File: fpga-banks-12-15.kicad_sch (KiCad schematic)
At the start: 1 part, among them U1 XC7K410T-2FFG900I

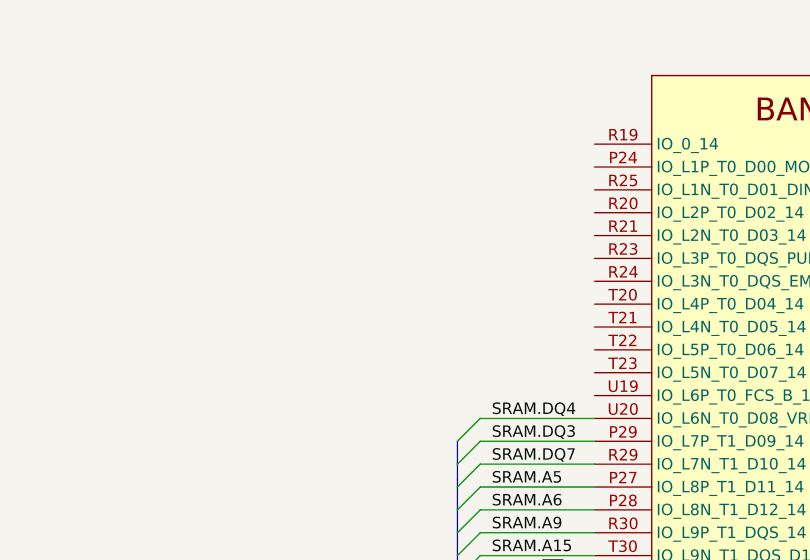
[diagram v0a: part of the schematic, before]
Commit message: Add SPI-FLASH bus and SPI Flash IC. Connet it to FPGA
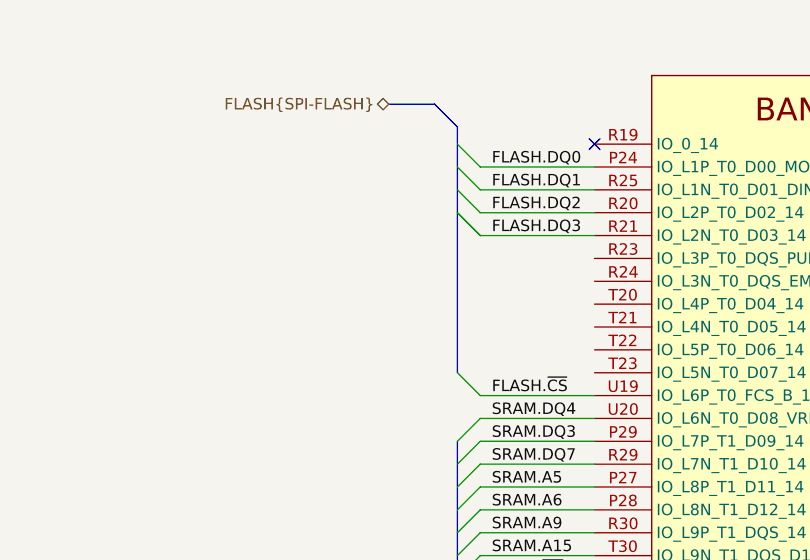
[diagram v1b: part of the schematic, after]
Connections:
- net FLASH.DQ0: now reaches U1.P24 (IO_L1P_T0_D00_MOSI_14)
- net FLASH.DQ2: now reaches U1.R20 (IO_L2P_T0_D02_14)
- net FLASH.DQ3: now reaches U1.R21 (IO_L2N_T0_D03_14)
- net FLASH.DQ1: now reaches U1.R25 (IO_L1N_T0_D01_DIN_14)
- net FLASH.~{CS}: now reaches U1.U19 (IO_L6P_T0_FCS_B_14)
- no-connect marks 6 -> 7
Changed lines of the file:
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@@
   )
   (no_connect (at 255.27 187.96))
+  (no_connect (at 255.27 76.2))
   (no_connect (at 255.27 154.94))
   (no_connect (at 255.27 190.5))
@@
     (stroke (width 0) (type default) (color 0 0 0 0))
   )
+  (bus_entry (at 240.03 78.74) (size 2.54 2.54)
+    (stroke (width 0) (type default) (color 0 0 0 0))
+  )
   (bus_entry (at 240.03 127) (size 2.54 -2.54)
     (stroke (width 0) (type default) (color 0 0 0 0))
   )
+  (bus_entry (at 240.03 76.2) (size 2.54 2.54)
+    (stroke (width 0) (type default) (color 0 0 0 0))
+  )
   (bus_entry (at 240.03 111.76) (size 2.54 -2.54)
     (stroke (width 0) (type default) (color 0 0 0 0))
   )
+  (bus_entry (at 242.57 104.14) (size -2.54 -2.54)
+    (stroke (width 0) (type default) (color 0 0 0 0))
+  )
   (bus_entry (at 240.03 167.64) (size 2.54 -2.54)
     (stroke (width 0) (type default) (color 0 0 0 0))
@@
     (stroke (width 0) (type default) (color 0 0 0 0))
   )
+  (bus_entry (at 240.03 83.82) (size 2.54 2.54)
+    (stroke (width 0) (type default) (color 0 0 0 0))
+  )
   (bus_entry (at 240.03 119.38) (size 2.54 -2.54)
     (stroke (width 0) (type default) (color 0 0 0 0))
@@
     (stroke (width 0) (type default) (color 0 0 0 0))
   )
+  (bus_entry (at 240.03 81.28) (size 2.54 2.54)
+    (stroke (width 0) (type default) (color 0 0 0 0))
+  )
   (bus_entry (at 240.03 185.42) (size 2.54 -2.54)
     (stroke (width 0) (type default) (color 0 0 0 0))
@@
     (stroke (width 0) (type default) (color 0 0 0 0))
   )
+  (bus_entry (at 240.03 83.82) (size 2.54 2.54)
+    (stroke (width 0) (type default) (color 0 0 0 0))
+  )
   (bus_entry (at 240.03 114.3) (size 2.54 -2.54)
     (stroke (width 0) (type default) (color 0 0 0 0))
@@
     (stroke (width 0) (type default) (color 0 0 0 0))
   )
+  (bus (pts (xy 240.03 78.74) (xy 240.03 81.28))
+    (stroke (width 0) (type default) (color 0 0 0 0))
+  )
   (bus (pts (xy 240.03 195.58) (xy 240.03 198.12))
     (stroke (width 0) (type default) (color 0 0 0 0))
@@
     (stroke (width 0) (type default) (color 0 0 0 0))
   )
+  (wire (pts (xy 242.57 78.74) (xy 255.27 78.74))
+    (stroke (width 0) (type default) (color 0 0 0 0))
+  )
   (wire (pts (xy 242.57 132.08) (xy 255.27 132.08))
     (stroke (width 0) (type default) (color 0 0 0 0))
@@
     (stroke (width 0) (type default) (color 0 0 0 0))
   )
+  (bus (pts (xy 232.41 71.755) (xy 237.49 71.755))
+    (stroke (width 0) (type default) (color 0 0 0 0))
+  )
   (wire (pts (xy 242.57 139.7) (xy 255.27 139.7))
     (stroke (width 0) (type default) (color 0 0 0 0))
@@
     (stroke (width 0) (type default) (color 0 0 0 0))
   )
+  (wire (pts (xy 242.57 104.14) (xy 255.27 104.14))
+    (stroke (width 0) (type default) (color 0 0 0 0))
+  )
   (bus (pts (xy 240.03 187.96) (xy 240.03 195.58))
     (stroke (width 0) (type default) (color 0 0 0 0))
@@
     (stroke (width 0) (type default) (color 0 0 0 0))
   )
+  (wire (pts (xy 242.57 83.82) (xy 255.27 83.82))
+    (stroke (width 0) (type default) (color 0 0 0 0))
+  )
   (wire (pts (xy 242.57 165.1) (xy 255.27 165.1))
     (stroke (width 0) (type default) (color 0 0 0 0))
   )
+  (wire (pts (xy 242.57 86.36) (xy 255.27 86.36))
+    (stroke (width 0) (type default) (color 0 0 0 0))
+  )
   (bus (pts (xy 240.03 160.02) (xy 240.03 162.56))
     (stroke (width 0) (type default) (color 0 0 0 0))
@@
     (stroke (width 0) (type default) (color 0 0 0 0))
   )
+  (bus (pts (xy 240.03 83.82) (xy 240.03 101.6))
+    (stroke (width 0) (type default) (color 0 0 0 0))
+  )
   (bus (pts (xy 240.03 139.7) (xy 240.03 142.24))
     (stroke (width 0) (type default) (color 0 0 0 0))
@@
     (stroke (width 0) (type default) (color 0 0 0 0))
   )
+  (bus (pts (xy 237.49 71.755) (xy 240.03 74.295))
+    (stroke (width 0) (type default) (color 0 0 0 0))
+  )
   (bus (pts (xy 240.03 137.16) (xy 240.03 139.7))
     (stroke (width 0) (type default) (color 0 0 0 0))
@@
     (stroke (width 0) (type default) (color 0 0 0 0))
   )
+  (bus (pts (xy 240.03 76.2) (xy 240.03 78.74))
+    (stroke (width 0) (type default) (color 0 0 0 0))
+  )
   (bus (pts (xy 240.03 116.84) (xy 240.03 119.38))
     (stroke (width 0) (type default) (color 0 0 0 0))
@@
     (stroke (width 0) (type default) (color 0 0 0 0))
   )
+  (bus (pts (xy 240.03 74.295) (xy 240.03 76.2))
+    (stroke (width 0) (type default) (color 0 0 0 0))
+  )
   (bus (pts (xy 240.03 162.56) (xy 240.03 165.1))
     (stroke (width 0) (type default) (color 0 0 0 0))
@@
     (stroke (width 0) (type default) (color 0 0 0 0))
   )
+  (bus (pts (xy 240.03 81.28) (xy 240.03 83.82))
+    (stroke (width 0) (type default) (color 0 0 0 0))
+  )
+  (wire (pts (xy 242.57 81.28) (xy 255.27 81.28))
+    (stroke (width 0) (type default) (color 0 0 0 0))
+  )
   (wire (pts (xy 242.57 137.16) (xy 255.27 137.16))
     (stroke (width 0) (type default) (color 0 0 0 0))
@@
     (effects (font (size 1.27 1.27)) (justify left bottom))
   )
+  (label "FLASH.DQ0" (at 243.84 78.74 0)
+    (effects (font (size 1.27 1.27)) (justify left bottom))
+  )
   (label "SRAM.A17" (at 244.475 177.8 0)
     (effects (font (size 1.27 1.27)) (justify left bottom))
@@
     (effects (font (size 1.27 1.27)) (justify left bottom))
   )
+  (label "FLASH.DQ2" (at 243.84 83.82 0)
+    (effects (font (size 1.27 1.27)) (justify left bottom))
+  )
   (label "SRAM.A19" (at 244.475 167.64 0)
     (effects (font (size 1.27 1.27)) (justify left bottom))
@@
     (effects (font (size 1.27 1.27)) (justify left bottom))
   )
+  (label "FLASH.~{CS}" (at 243.84 104.14 0)
+    (effects (font (size 1.27 1.27)) (justify left bottom))
+  )
   (label "SRAM.A5" (at 243.84 114.3 0)
     (effects (font (size 1.27 1.27)) (justify left bottom))
   )
+  (label "FLASH.DQ1" (at 243.84 81.28 0)
+    (effects (font (size 1.27 1.27)) (justify left bottom))
+  )
   (label "SRAM.CE2" (at 244.475 180.34 0)
     (effects (font (size 1.27 1.27)) (justify left bottom))
   )
+  (label "FLASH.DQ3" (at 243.84 86.36 0)
+    (effects (font (size 1.27 1.27)) (justify left bottom))
+  )
   (label "SRAM.A6" (at 243.84 116.84 0)
     (effects (font (size 1.27 1.27)) (justify left bottom))
@@
     (effects (font (size 1.27 1.27)) (justify left bottom))
   )
+  (hierarchical_label "FLASH{SPI-FLASH}" (shape bidirectional) (at 232.41 71.755 180)
+    (effects (font (size 1.27 1.27)) (justify right))
+  )
   (hierarchical_label "SRAM{SRAM}" (shape input) (at 220.98 208.915 180)
